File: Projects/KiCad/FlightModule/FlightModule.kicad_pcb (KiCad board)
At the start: 2 copper layers, 110 x 95 mm, 58 parts, among them J1 Conn_01x05_Socket, J2 Conn_01x04_Pin, J3 Conn_01x05_Pin, J4 Conn_01x02_Pin, J5 Conn_01x02_Pin, J6 Conn_01x02_Pin, J7 Conn_01x02_Pin, J8 Conn_01x02_Pin, SW1 SW_Push, SW2 SW_Push, U1 NUCLEO-F303K8, U2 MCP2562-E-P, U3 TLP222A, U4 TLP222A, U5 MB85RS2MT

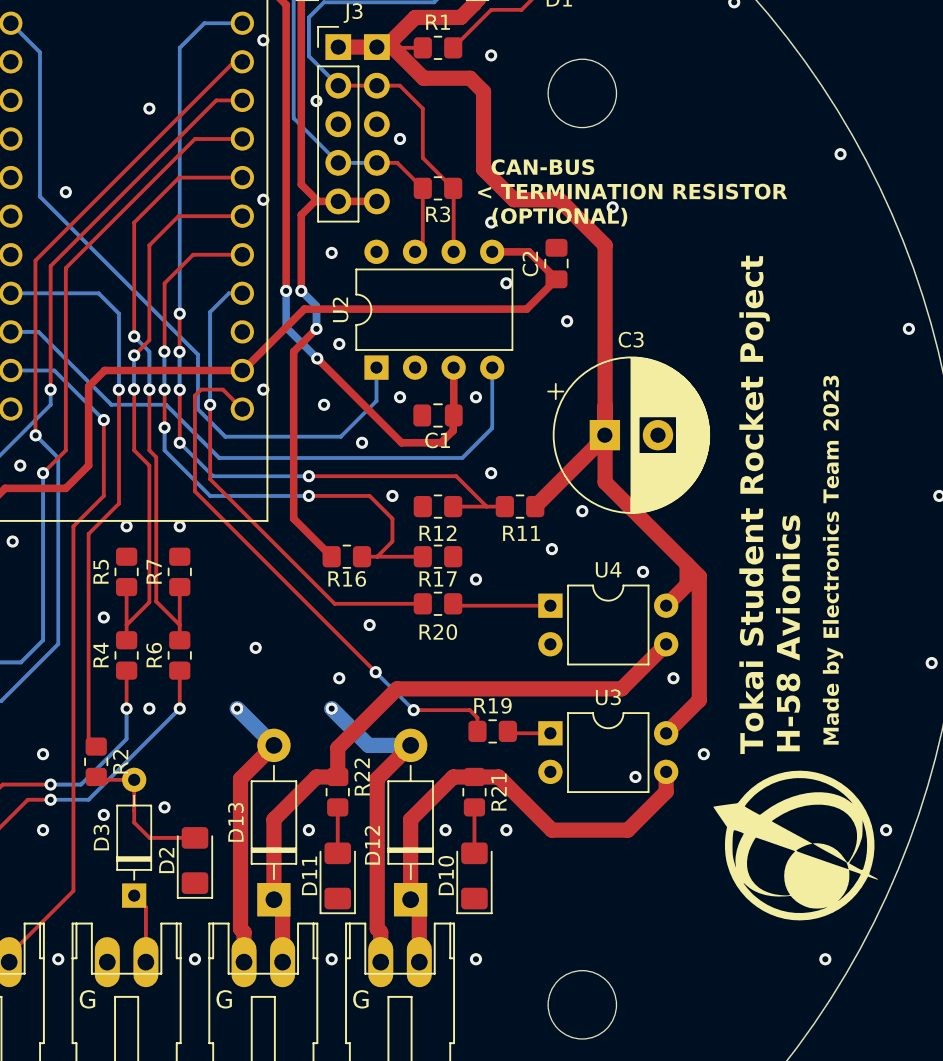
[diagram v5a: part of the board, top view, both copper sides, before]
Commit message: ソレノイドのサージキラー回路に整流用ダイオードを追加
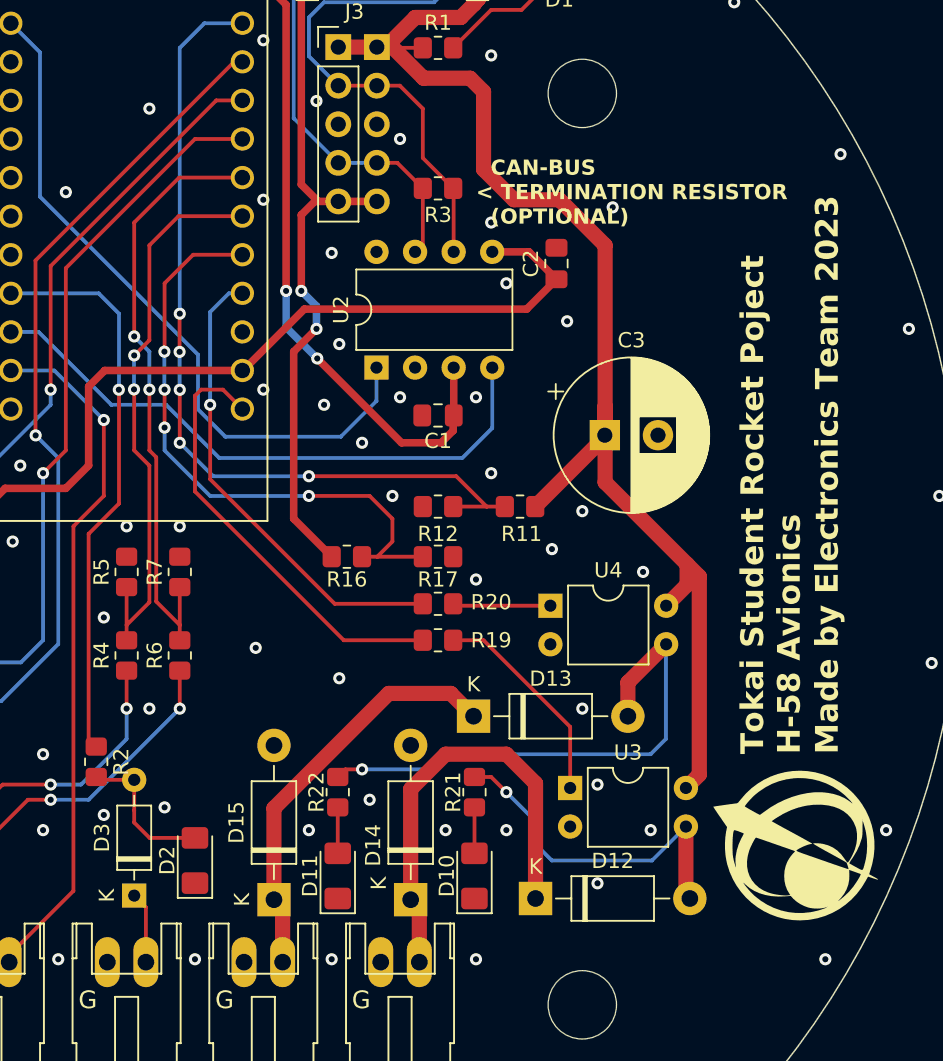
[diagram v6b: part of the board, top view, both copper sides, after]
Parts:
- added D12: 1N4007, Diode_THT:D_DO-41_SOD81_P10.16mm_Horizontal, F.Cu at (175.4, 128.0)
- added D13: 1N4007, Diode_THT:D_DO-41_SOD81_P10.16mm_Horizontal, F.Cu at (171.3, 116.0)
- moved R19 7.00 mm to (169.0, 111.0)
- moved U3 3.83 mm to (177.7, 120.7)
- renumbered D12 to D14, D13 to D15
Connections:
- R21 pad 1: Net-(D12-K) -> Net-(D12-A)
- R22 pad 1: Net-(D13-K) -> Net-(D13-A)
- U3 pad 3: Net-(D12-K) -> Net-(D12-A)
- U4 pad 3: Net-(D13-K) -> Net-(D13-A)
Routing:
- net GND: track 40.2 -> 0.00 mm, vias 98 -> 97
- net Net-(D13-A): track 0.00 -> 34.7 mm, vias 0 -> 1
- net Net-(D12-A): track 0.00 -> 22.8 mm, vias 0 -> 1
- net Net-(D13-K): track 41.3 -> 27.3 mm
- net Net-(R19-Pad2): track 2.85 -> 14.1 mm
- net CONTROL_SEPARATOR_0: track 35.8 -> 29.2 mm, vias 2 -> 0
- net SOLENOID_POWER: track 106.1 -> 109.2 mm
- net Net-(D12-K): track 31.4 -> 29.2 mm

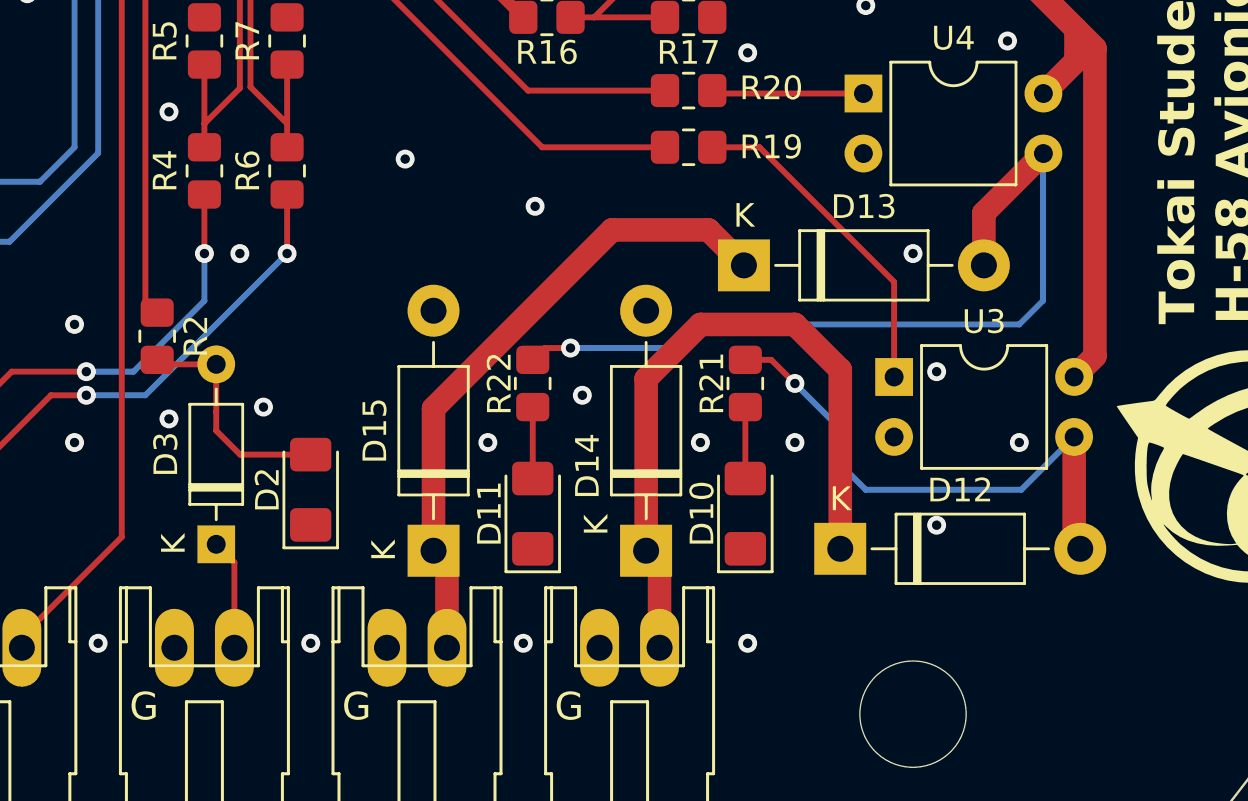
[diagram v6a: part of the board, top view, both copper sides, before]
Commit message: ダイオードをSMDに変更
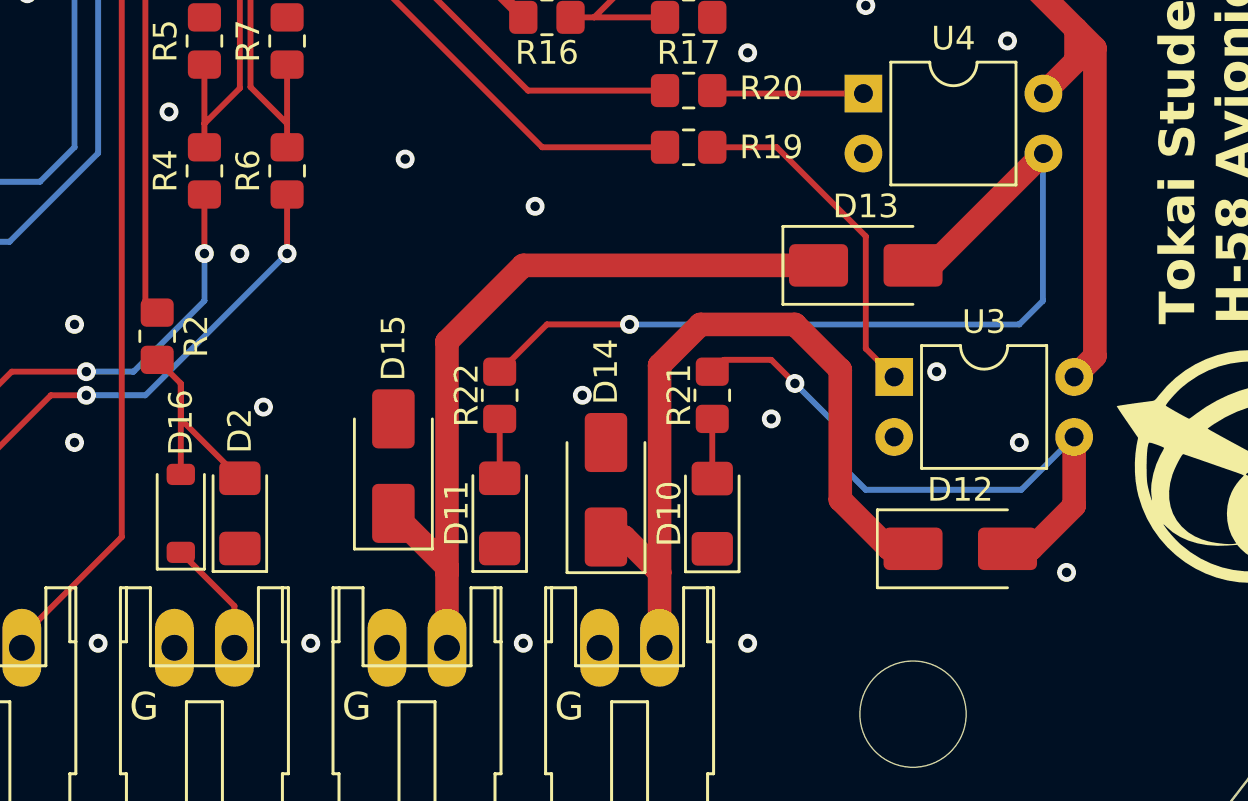
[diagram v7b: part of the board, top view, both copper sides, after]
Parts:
- removed D3: 1N4148, Diode_THT:D_DO-35_SOD27_P7.62mm_Horizontal
- added D16: MMSD4148, Diode_SMD:D_SOD-123, F.Cu at (147.5, 126.5)
- D12, D13, D14, D15: value 1N4007 -> NRVA4007T3G; footprint Diode_THT:D_DO-41_SOD81_P10.16mm_Horizontal -> Diode_SMD:D_SMA
- moved D13 5.16 mm to (176.5, 116.0)
- moved D12 5.08 mm to (180.5, 128.0)
- moved D15 3.96 mm to (156.5, 124.5)
- moved D2 3.16 mm to (150.0, 126.5)
- moved D14 3.09 mm to (165.5, 125.5)
- moved R21 1.49 mm to (170.0, 121.5)
- moved R22 1.49 mm to (161.0, 121.5)
- moved D11 1.40 mm to (161.0, 126.5)
- moved D10 1.40 mm to (170.0, 126.5)
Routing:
- net Net-(D13-K): track 27.3 -> 33.5 mm
- net Net-(D12-K): track 29.2 -> 33.5 mm
- net Net-(D13-A): track 34.7 -> 38.0 mm
- net Net-(D12-A): track 22.8 -> 26.1 mm
- net Net-(D11-A): track 3.03 -> 2.51 mm
- net Net-(D10-A): track 3.03 -> 2.53 mm
- net GND: vias 97 -> 93

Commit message: 一通り部品を選定
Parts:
- removed D15: NRVA4007T3G, Diode_SMD:D_SMA
- removed D16: MMSD4148, Diode_SMD:D_SOD-123
- added D11: 1N4007, Diode_SMD:D_SOD-123F, F.Cu at (180.5, 128.0)
- added R23: 120Ω, Resistor_SMD:R_0603_1608Metric_Pad0.98x0.95mm_HandSolder, F.Cu at (169.5, 113.0)
- added R24: 120Ω, Resistor_SMD:R_0603_1608Metric_Pad0.98x0.95mm_HandSolder, F.Cu at (169.5, 109.5)
- C3: value 470μF -> 100μF; footprint Capacitor_THT:CP_Radial_D10.0mm_P3.50mm -> Capacitor_SMD:CP_Elec_6.3x7.7
- D1, D2: value LED -> RED; footprint LED_SMD:LED_1206_3216Metric_Pad1.42x1.75mm_HandSolder -> LED_SMD:LED_0603_1608Metric_Pad1.05x0.95mm_HandSolder
- D10: renamed from D11; value LED -> GREEN; footprint LED_SMD:LED_1206_3216Metric_Pad1.42x1.75mm_HandSolder -> LED_SMD:LED_0603_1608Metric_Pad1.05x0.95mm_HandSolder
- D12, D13, D14: value NRVA4007T3G -> 1N4007; footprint Diode_SMD:D_SMA -> Diode_SMD:D_SOD-123F
- D3: renamed from D4; value LED -> GREEN; footprint LED_SMD:LED_1206_3216Metric_Pad1.42x1.75mm_HandSolder -> LED_SMD:LED_0603_1608Metric_Pad1.05x0.95mm_HandSolder
- D4: renamed from D5; value LED -> GREEN; footprint LED_SMD:LED_1206_3216Metric_Pad1.42x1.75mm_HandSolder -> LED_SMD:LED_0603_1608Metric_Pad1.05x0.95mm_HandSolder
- D5: renamed from D6; value LED -> GREEN; footprint LED_SMD:LED_1206_3216Metric_Pad1.42x1.75mm_HandSolder -> LED_SMD:LED_0603_1608Metric_Pad1.05x0.95mm_HandSolder
- D6: renamed from D7; value LED -> GREEN; footprint LED_SMD:LED_1206_3216Metric_Pad1.42x1.75mm_HandSolder -> LED_SMD:LED_0603_1608Metric_Pad1.05x0.95mm_HandSolder
- D7: renamed from D8; value LED -> ORANGE; footprint LED_SMD:LED_1206_3216Metric_Pad1.42x1.75mm_HandSolder -> LED_SMD:LED_0603_1608Metric_Pad1.05x0.95mm_HandSolder
- D8: renamed from D9; value LED -> ORANGE; footprint LED_SMD:LED_1206_3216Metric_Pad1.42x1.75mm_HandSolder -> LED_SMD:LED_0603_1608Metric_Pad1.05x0.95mm_HandSolder
- D9: renamed from D10; value LED -> GREEN; footprint LED_SMD:LED_1206_3216Metric_Pad1.42x1.75mm_HandSolder -> LED_SMD:LED_0603_1608Metric_Pad1.05x0.95mm_HandSolder
- R1, R14, R15, R18, R21, R22, R3: footprint Resistor_SMD:R_0805_2012Metric_Pad1.20x1.40mm_HandSolder -> Resistor_SMD:R_0603_1608Metric_Pad0.98x0.95mm_HandSolder
- R10, R13, R8, R9: value 100Ω -> 300Ω; footprint Resistor_SMD:R_0805_2012Metric_Pad1.20x1.40mm_HandSolder -> Resistor_SMD:R_0603_1608Metric_Pad0.98x0.95mm_HandSolder
- R11: value ?Ω -> 3kΩ; footprint Resistor_SMD:R_0805_2012Metric_Pad1.20x1.40mm_HandSolder -> Resistor_SMD:R_0603_1608Metric_Pad0.98x0.95mm_HandSolder
- R12: value ?Ω -> 750Ω; footprint Resistor_SMD:R_0805_2012Metric_Pad1.20x1.40mm_HandSolder -> Resistor_SMD:R_0603_1608Metric_Pad0.98x0.95mm_HandSolder
- R16: value ?Ω -> 1.3kΩ; footprint Resistor_SMD:R_0805_2012Metric_Pad1.20x1.40mm_HandSolder -> Resistor_SMD:R_0603_1608Metric_Pad0.98x0.95mm_HandSolder
- R17: value ?Ω -> 1.2kΩ; footprint Resistor_SMD:R_0805_2012Metric_Pad1.20x1.40mm_HandSolder -> Resistor_SMD:R_0603_1608Metric_Pad0.98x0.95mm_HandSolder
- R19, R20: value 100Ω -> 120Ω; footprint Resistor_SMD:R_0805_2012Metric_Pad1.20x1.40mm_HandSolder -> Resistor_SMD:R_0603_1608Metric_Pad0.98x0.95mm_HandSolder
- R2: value 330Ω -> 300Ω; footprint Resistor_SMD:R_0805_2012Metric_Pad1.20x1.40mm_HandSolder -> Resistor_SMD:R_0603_1608Metric_Pad0.98x0.95mm_HandSolder
- R4: value ?Ω -> 4.3kΩ; footprint Resistor_SMD:R_0805_2012Metric_Pad1.20x1.40mm_HandSolder -> Resistor_SMD:R_0603_1608Metric_Pad0.98x0.95mm_HandSolder
- R5, R7: value ?Ω -> 820Ω; footprint Resistor_SMD:R_0805_2012Metric_Pad1.20x1.40mm_HandSolder -> Resistor_SMD:R_0603_1608Metric_Pad0.98x0.95mm_HandSolder
- R6: value ?Ω -> 5.6kΩ; footprint Resistor_SMD:R_0805_2012Metric_Pad1.20x1.40mm_HandSolder -> Resistor_SMD:R_0603_1608Metric_Pad0.98x0.95mm_HandSolder
- moved D13 13.8 mm to (166.0, 125.0), turned to 90 degrees
- moved D12 12.6 mm to (176.5, 116.0)
- moved D14 8.51 mm to (157.0, 125.0)
- moved R19 4.12 mm to (165.0, 112.0)
- moved R20 4.00 mm to (165.0, 108.5)
- moved C3 2.63 mm to (180.8, 95.0)
- moved D1 0.49 mm to (176.5, 67.0)
- moved D5 0.44 mm to (112.1, 91.2)
- moved D3 0.31 mm to (112.0, 85.2)
- moved D4 0.31 mm to (112.0, 88.2)
- moved D6 0.31 mm to (112.0, 94.2)
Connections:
- D13 pad 1: Net-(D13-K) -> Net-(D11-K)
- D13 pad 2: Net-(D13-A) -> GND
- D2 pad 2: Net-(D16-A) -> Net-(D2-A)
- J4 pad 2: Net-(D16-K) -> Net-(D2-A)
- J7 pad 2: Net-(D12-K) -> Net-(D11-K)
- J8 pad 2: Net-(D13-K) -> Net-(D12-K)
- R2 pad 2: Net-(D16-A) -> Net-(D2-A)
- R21 pad 1: Net-(D12-A) -> Net-(D11-A)
- R22 pad 1: Net-(D13-A) -> Net-(D12-A)
- U3 pad 3: Net-(D12-A) -> Net-(D11-A)
- U4 pad 3: Net-(D13-A) -> Net-(D12-A)
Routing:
- net Net-(D13-A): track 38.0 -> 0.00 mm, vias 1 -> 0
- net Net-(D11-K): track 0.00 -> 34.5 mm
- net Net-(D13-K): track 33.5 -> 0.00 mm
- net Net-(D11-A): track 0.00 -> 26.7 mm, vias 0 -> 1
- net Net-(D2-A): track 0.00 -> 19.2 mm
- net Net-(D12-A): track 26.1 -> 38.6 mm
- net Net-(D16-A): track 10.3 -> 0.00 mm
- net Net-(R20-Pad2): track 6.45 -> 12.3 mm
- net Net-(R19-Pad2): track 14.5 -> 20.0 mm
- net Net-(D16-K): track 4.98 -> 0.00 mm
- net CONTROL_SEPARATOR_1: track 31.0 -> 27.0 mm
- net CONTROL_SEPARATOR_0: track 29.2 -> 25.6 mm
- net SOLENOID_POWER: track 109.2 -> 110.5 mm
- net Net-(D9-A): track 2.53 -> 3.14 mm
- net Net-(D10-A): track 2.51 -> 3.12 mm
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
